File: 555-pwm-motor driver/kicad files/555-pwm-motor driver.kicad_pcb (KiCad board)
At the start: 2 copper layers, 17 parts, among them J1 Screw_Terminal_01x02, J2 Screw_Terminal_01x02, Q1 IRLZ44N, U1 LM7805_TO220, U2 SE555P, U3 3PIN-POT-LOCAL

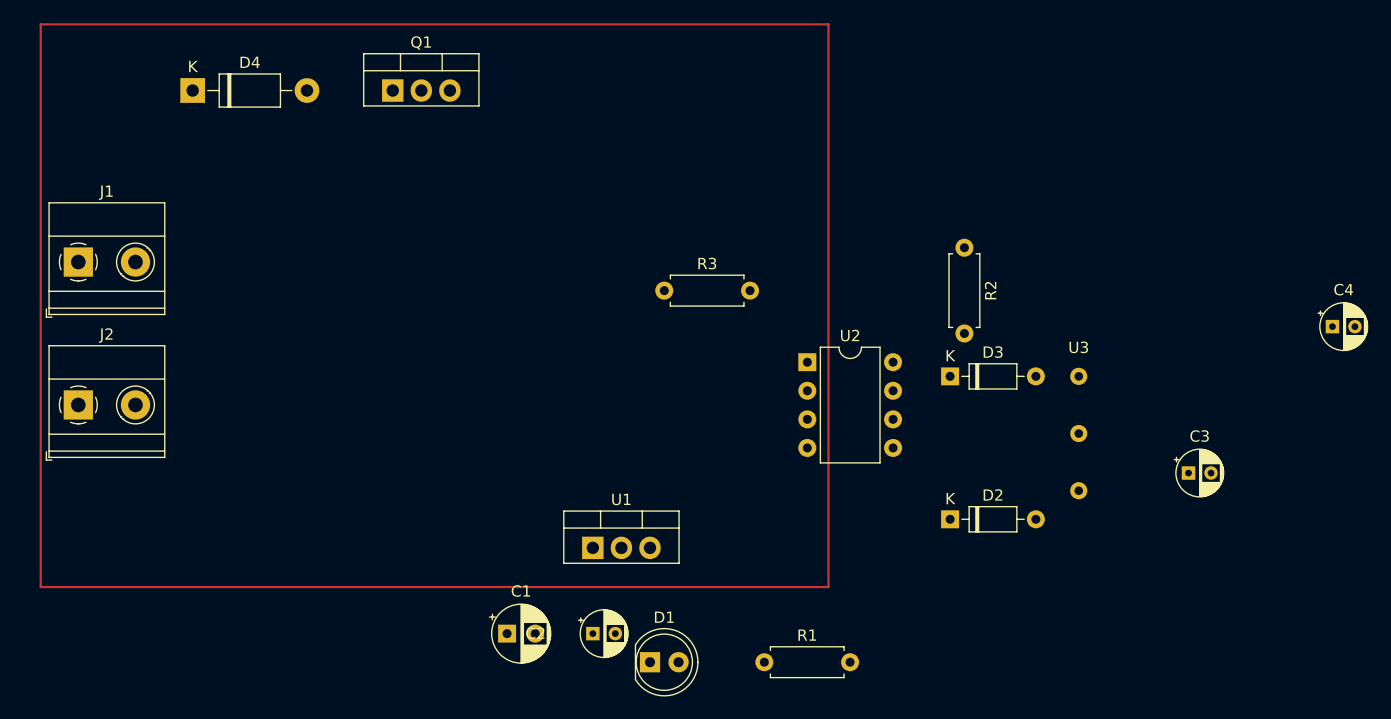
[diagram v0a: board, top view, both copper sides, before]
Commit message: Adding routing
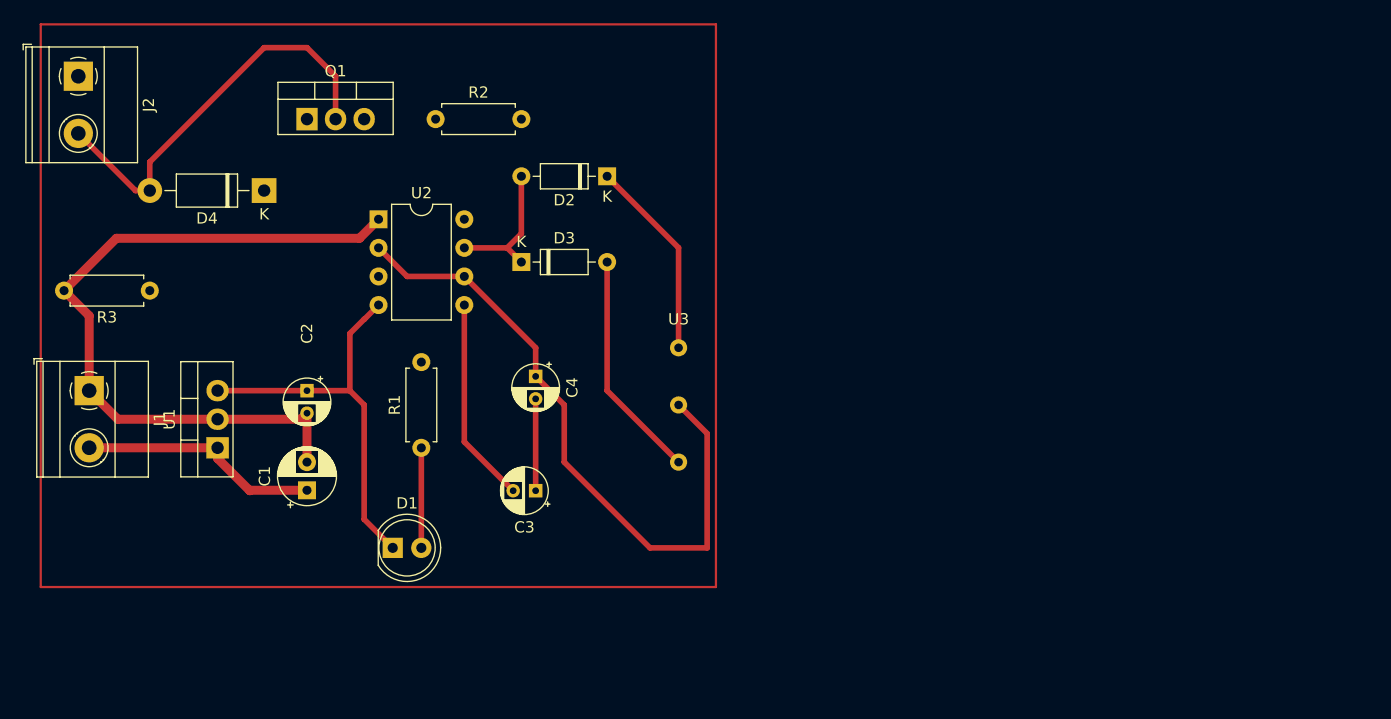
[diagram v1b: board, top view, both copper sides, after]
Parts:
- moved C4 70.9 mm to (94.0, 81.3), turned to -90 degrees
- moved C3 58.0 mm to (94.0, 91.4), turned to 180 degrees
- moved R2 48.4 mm to (85.1, 58.4), turned to 0 degrees
- moved R3 45.7 mm to (59.7, 73.7), turned to 180 degrees
- moved D2 43.1 mm to (100.3, 63.5), turned to 180 degrees
- moved U2 40.2 mm to (80.0, 67.3)
- moved D3 39.4 mm to (92.7, 71.1)
- moved R1 35.9 mm to (83.8, 87.6), turned to 90 degrees
- moved U3 35.7 mm to (106.7, 83.8)
- moved U1 34.5 mm to (65.7, 87.6), turned to 90 degrees
- moved C2 33.3 mm to (73.7, 82.5), turned to -90 degrees
- moved J2 29.2 mm to (53.3, 54.6), turned to -90 degrees
- moved D1 25.0 mm to (81.3, 96.5)
- moved C1 21.9 mm to (73.7, 91.4), turned to 90 degrees
- moved J1 11.5 mm to (54.3, 82.5), turned to -90 degrees
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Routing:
- net GND: track 0.00 -> 73.5 mm
- net Net-(C4-Pad1): track 0.00 -> 58.5 mm
- net Net-(D4-Pad2): track 0.00 -> 36.6 mm
- net 5V: track 0.00 -> 36.0 mm
- net 12V: track 0.00 -> 21.5 mm
- net Net-(D3-Pad2): track 0.00 -> 20.4 mm
- net Net-(C3-Pad2): track 0.00 -> 18.3 mm
- net Net-(D2-Pad1): track 0.00 -> 17.9 mm
- net Net-(D2-Pad2): track 0.00 -> 12.5 mm
- net Net-(D1-Pad2): track 0.00 -> 8.89 mm

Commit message: Adding pcb files-closes #1
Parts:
- added J3: Conn_01x01_Male, Connector_PinHeader_1.00mm:PinHeader_1x01_P1.00mm_Vertical, F.Cu at (76.2, 69.8)
- added J4: Conn_01x01_Male, Connector_PinHeader_1.00mm:PinHeader_1x01_P1.00mm_Vertical, F.Cu at (90.2, 73.7)
- moved C1 14.3 mm to (63.5, 81.3), turned to 180 degrees
- moved U1 14.1 mm to (63.5, 73.7), turned to 180 degrees
- moved R3 12.8 mm to (72.4, 74.9), turned to 90 degrees
- moved D4 12.5 mm to (64.8, 53.3), turned to 0 degrees
- moved J1 8.93 mm to (58.4, 90.5), turned to 0 degrees
- moved Q1 7.93 mm to (67.3, 63.2)
- moved C2 6.48 mm to (72.4, 88.9)
- moved C4 6.35 mm to (97.8, 86.4)
- moved C3 5.39 mm to (90.2, 87.6), turned to 0 degrees
- moved R2 3.59 mm to (87.6, 55.9)
- moved J2 2.24 mm to (55.6, 54.6)
- moved U3 1.80 mm to (105.4, 85.1)
- moved D3 1.27 mm to (92.7, 69.8)
- turned D2 to 90 degrees
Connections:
- U2 pad 2: Net-(C4-Pad1) -> Net-(J3-Pad1)
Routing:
- net 5V: track 36.0 -> 113.1 mm
- net GND: track 73.5 -> 11.1 mm
- net 12V: track 21.5 -> 56.1 mm
- net Net-(C4-Pad1): track 58.5 -> 27.1 mm
- net Q: track 0.00 -> 22.5 mm
- net Net-(D2-Pad2): track 12.5 -> 25.2 mm
- net Net-(D4-Pad2): track 36.6 -> 28.5 mm
- net Net-(D3-Pad2): track 20.4 -> 27.5 mm
- net Net-(D2-Pad1): track 17.9 -> 21.9 mm
- net Net-(J3-Pad1): track 0.00 -> 3.82 mm
- net Net-(C3-Pad2): track 18.3 -> 14.6 mm
- added copper zone on F.Cu, net GND

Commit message: Cleaning up pcb
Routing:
- net GND: track 11.1 -> 1.31 mm

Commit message: Cleaning up pcb
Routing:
- net GND: track 1.31 -> 0.00 mm
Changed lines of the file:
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@@
   (segment (start 52.07 55.88) (end 53.345 54.605) (width 1) (layer "F.Cu") (net 1))
   (segment (start 55.575 54.605) (end 63.505 54.605) (width 1) (layer "F.Cu") (net 1))
-  (segment (start 61 81.28) (end 59.69 81.28) (width 1) (layer "F.Cu") (net 2))
   (segment (start 87.63 55.88) (end 87.63 67.31) (width 0.8) (layer "F.Cu") (net 3))
   (segment (start 72.39 88.9) (end 72.39 80.01) (width 0.8) (layer "F.Cu") (net 3))
@@
   (segment (start 80.02 74.94) (end 87.64 67.32) (width 0.8) (layer "F.Cu") (net 3))
   (segment (start 52.07 96.52) (end 53.34 97.79) (width 0.8) (layer "F.Cu") (net 3))
-  (segment (start 87.64 74.94) (end 87.64 83.1) (width 0.8) (layer "F.Cu") (net 4))
-  (segment (start 87.64 83.1) (end 92.17 87.63) (width 0.8) (layer "F.Cu") (net 4))
+  (segment (start 92.17 85.82) (end 92.17 87.63) (width 0.8) (layer "F.Cu") (net 4))
+  (segment (start 87.64 74.94) (end 87.64 81.29) (width 0.8) (layer "F.Cu") (net 4))
+  (segment (start 87.64 81.29) (end 92.17 85.82) (width 0.8) (layer "F.Cu") (net 4))
   (segment (start 97.79 86.36) (end 104.14 86.36) (width 0.8) (layer "F.Cu") (net 5))
   (segment (start 90.17 78.74) (end 97.79 86.36) (width 0.8) (layer "F.Cu") (net 5))
